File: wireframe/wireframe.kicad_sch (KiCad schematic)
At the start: 37 parts, among them U1 ESP32-S2-DevKitC-1

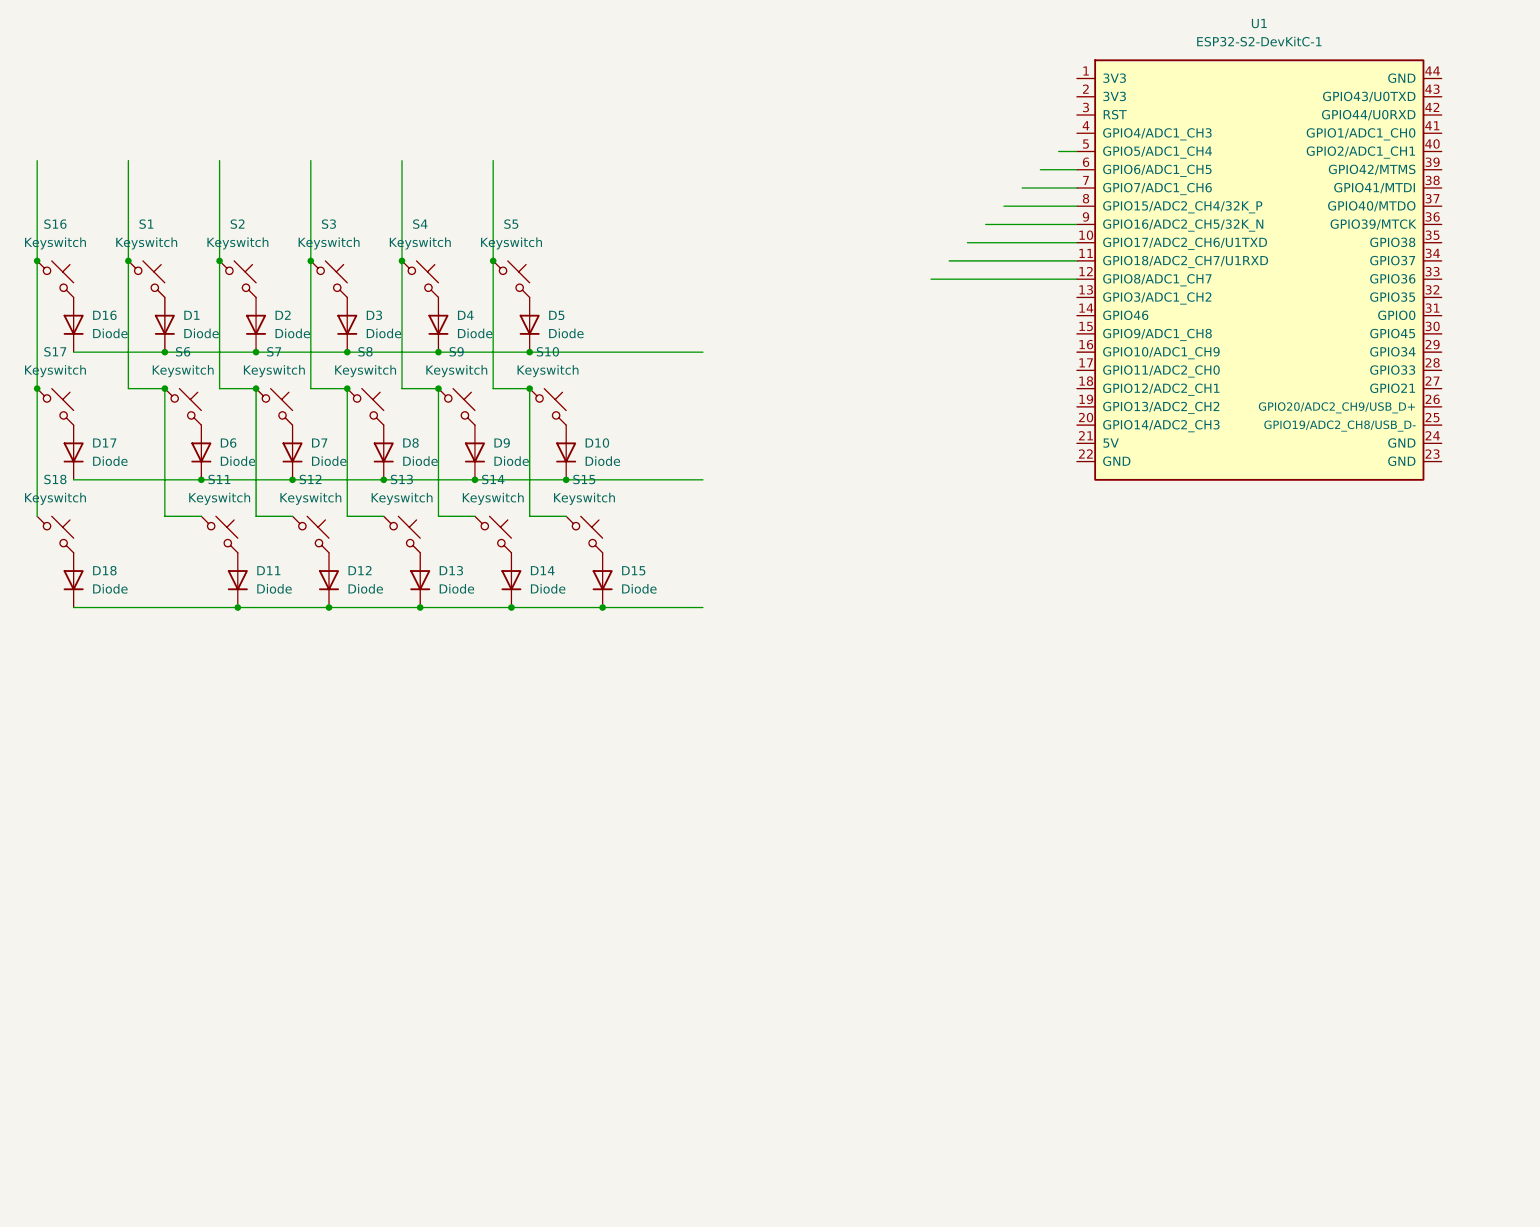
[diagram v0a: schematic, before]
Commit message: Finalize layout and fully traced to ESP32
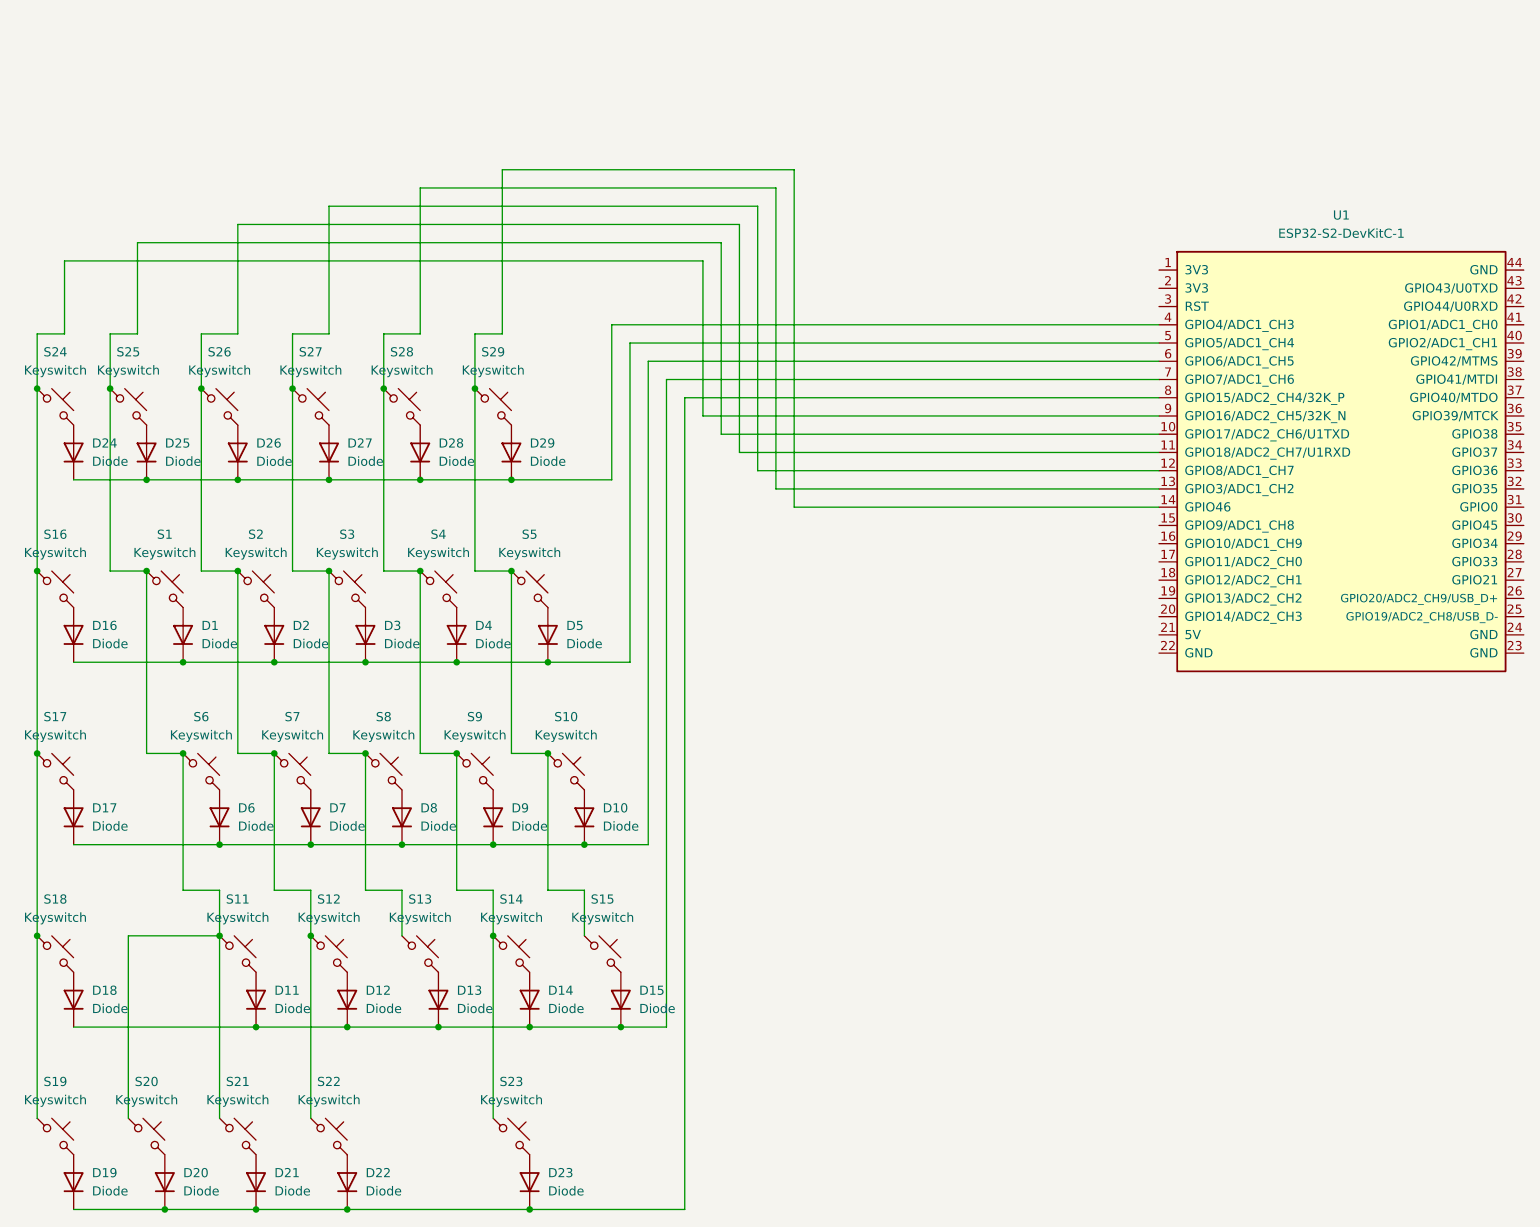
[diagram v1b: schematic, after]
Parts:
- added D19, D20, D21, D22, D23, D24, D25, D26, D27, D28, D29: Diode, ScottoKeebs_Components:Diode_DO-35, symbol ScottoKeebs:Placeholder_Diode
- added S19, S20, S21, S22, S24, S25, S26, S27, S28, S29: Keyswitch, ScottoKeebs_MX:MX_PCB_1.00u, symbol ScottoKeebs:Placeholder_Keyswitch
- added S23: Keyswitch, ScottoKeebs_MX:MX_PCB_3.00u, symbol ScottoKeebs:Placeholder_Keyswitch
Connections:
- net at S10.1, S15.1, S5.1: now also U1.14 (GPIO46), S29.1
- net at S14.1, S4.1, S9.1: now also U1.13 (GPIO3/ADC1_CH2), S23.1, S28.1
- net at S13.1, S3.1, S8.1: now also U1.12 (GPIO8/ADC1_CH7), S27.1
- net at D11.1 (K), D12.1 (K), D13.1 (K)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: now also U1.7 (GPIO7/ADC1_CH6)
- net at S16.1, S17.1, S18.1: now also U1.9 (GPIO16/ADC2_CH5/32K_N), S19.1, S24.1
- net at S12.1, S2.1, S7.1: now also U1.11 (GPIO18/ADC2_CH7/U1RXD), S22.1, S26.1
- net at D10.1 (K), D17.1 (K), D6.1 (K)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: now also U1.6 (GPIO6/ADC1_CH5)
- net at D1.1 (K), D16.1 (K), D2.1 (K)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: now also U1.5 (GPIO5/ADC1_CH4)
- net at S1.1, S11.1, S6.1: now also U1.10 (GPIO17/ADC2_CH6/U1TXD), S20.1, S21.1, S25.1
- net at U1.4 (GPIO4/ADC1_CH3): now also D24.1 (K), D25.1 (K), D26.1 (K), D27.1 (K), D28.1 (K), D29.1 (K)
- net at U1.8 (GPIO15/ADC2_CH4/32K_P): now also D19.1 (K), D20.1 (K), D21.1 (K), D22.1 (K), D23.1 (K)
- new net: D23.2 (A), S23.2
- new net: D20.2 (A), S20.2
- new net: D19.2 (A), S19.2
- new net: D26.2 (A), S26.2
- new net: D25.2 (A), S25.2
- new net: D22.2 (A), S22.2
- new net: D28.2 (A), S28.2
- new net: D24.2 (A), S24.2
- new net: D21.2 (A), S21.2
- new net: D27.2 (A), S27.2
- new net: D29.2 (A), S29.2
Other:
- moved on the sheet: D1, D10, D11, D12, D13, D14, D15, D16, D17, D18, D2, D3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
